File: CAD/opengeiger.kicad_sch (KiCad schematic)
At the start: 59 parts, among them J1 Conn_01x02, J10 Conn_01x04, J2 Conn_01x02, J3 Conn_01x06, J4 Conn_01x02, J5 Conn_01x04, J6 Conn_01x04, J7 Conn_01x02, J8 USB_C_Receptacle_USB2.0, J9 Conn_01x04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

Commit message: Feat:Added schematics, and updated readme
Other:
- company: (none) -> EIK IDEVERKSTED OPENGEIGER
- title: (none) -> Main Schematic
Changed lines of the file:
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@@
 (kicad_sch (version 20211123) (generator eeschema)
   (paper "A4")
+  (title_block
+    (title "Main Schematic")
+    (date "2022-11-03")
+    (rev "V.0.1.0")
+    (company "EIK IDEVERKSTED OPENGEIGER")
+  )
   (junction (at 130.81 33.02) (diameter 0) (color 0 0 0 0)
   )

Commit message: feat: added interactive html bom
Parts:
- added R18: 10k, Resistor_SMD:R_0603_1608Metric_Pad0.98x0.95mm_HandSolder, symbol Device:R
- Q3: value PMBT2222A,215 -> SI2301; MPN PMBT2222A,215 -> SI2302CDS-T1-GE3; Supplier Part Number 1727-2956-6-ND -> SI2302CDS-T1-GE3DKR-ND
- U2: INFO MOUSER -> DIGIKEY; Supplier Part Number 621-AP7361C-33ER-13 -> 576-1274-6-ND
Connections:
- net CLICKER: now also R18.2
- net GNDREF: now also R18.1
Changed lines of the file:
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@@
   (junction (at 41.91 104.14) (diameter 0) (color 0 0 0 0)
   )
+  (junction (at 198.12 62.23) (diameter 0) (color 0 0 0 0)
+  )
   (junction (at 158.75 165.1) (diameter 0) (color 0 0 0 0)
   )
@@
     (stroke (width 0) (type default) (color 0 0 0 0))
   )
+  (wire (pts (xy 198.12 62.23) (xy 200.66 62.23))
+    (stroke (width 0) (type default) (color 0 0 0 0))
+  )
   (wire (pts (xy 83.82 153.67) (xy 101.6 153.67))
     (stroke (width 0) (type default) (color 0 0 0 0))
@@
     (stroke (width 0) (type default) (color 0 0 0 0))
   )
+  (wire (pts (xy 198.12 63.5) (xy 198.12 62.23))
+    (stroke (width 0) (type default) (color 0 0 0 0))
+  )
   (wire (pts (xy 152.4 41.91) (xy 154.94 41.91))
     (stroke (width 0) (type default) (color 0 0 0 0))
@@
     (stroke (width 0) (type default) (color 0 0 0 0))
   )
+  (wire (pts (xy 195.58 62.23) (xy 198.12 62.23))
+    (stroke (width 0) (type default) (color 0 0 0 0))
+  )
   (wire (pts (xy 167.64 30.48) (xy 180.34 30.48))
     (stroke (width 0) (type default) (color 0 0 0 0))
@@
     )
   )
-  (global_label "CLICKER" (shape input) (at 200.66 62.23 180) (fields_autoplaced)
+  (global_label "CLICKER" (shape input) (at 195.58 62.23 180) (fields_autoplaced)
     (effects (font (size 1.27 1.27)) (justify right))
-    (property "Intersheet References" "${INTERSHEET_REFS}" (id 0) (at 190.385 62.1506 0)
+    (property "Intersheet References" "${INTERSHEET_REFS}" (id 0) (at 185.305 62.1506 0)
       (effects (font (size 1.27 1.27)) (justify right) hide)
     )
@@
       (effects (font (size 1.27 1.27) italic) hide)
     )
-    (property "Datasheet" "https://www.diodes.com/assets/Datasheets/AP7361C.pdf" (id 3) (at 59.69 105.41 0)
+    (property "Datasheet" "https://ww1.microchip.com/downloads/en/DeviceDoc/20005720A.pdf" (id 3) (at 59.69 105.41 0)
       (effects (font (size 1.27 1.27)) hide)
     )
@@
       (effects (font (size 1.27 1.27)) hide)
     )
-    (property "INFO" "MOUSER" (id 5) (at 59.69 104.14 0)
+    (property "INFO" "DIGIKEY" (id 5) (at 59.69 104.14 0)
       (effects (font (size 1.27 1.27)) hide)
     )
-    (property "Supplier Part Number" "621-AP7361C-33ER-13 " (id 6) (at 59.69 104.14 0)
+    (property "Supplier Part Number" "576-1274-6-ND" (id 6) (at 59.69 104.14 0)
       (effects (font (size 1.27 1.27)) hide)
     )
@@
     (pin "2")
   )
+  (symbol (lib_id "power:GNDREF") (at 198.12 71.12 0) (unit 1)
+    (in_bom yes) (on_board yes) (fields_autoplaced)
+    (property "Reference" "#PWR0112" (id 0) (at 198.12 77.47 0)
+      (effects (font (size 1.27 1.27)) hide)
+    )
+    (property "Value" "GNDREF" (id 1) (at 198.12 76.2 0))
+    (property "Footprint" "" (id 2) (at 198.12 71.12 0)
+      (effects (font (size 1.27 1.27)) hide)
+    )
+    (property "Datasheet" "" (id 3) (at 198.12 71.12 0)
+      (effects (font (size 1.27 1.27)) hide)
+    )
+    (pin "1")
+  )
   (symbol (lib_id "power:+3.3V") (at 87.63 21.59 0) (unit 1)
     (in_bom yes) (on_board yes) (fields_autoplaced)
@@
       (effects (font (size 1.27 1.27)) (justify left))
     )
-    (property "Value" "PMBT2222A,215" (id 1) (at 209.55 63.4999 0)
+    (property "Value" "SI2301" (id 1) (at 209.55 63.4999 0)
       (effects (font (size 1.27 1.27)) (justify left))
     )
@@
       (effects (font (size 1.27 1.27) italic) (justify left) hide)
     )
-    (property "Datasheet" "https://no.mouser.com/datasheet/2/916/PMBT2222A-2885992.pdf" (id 3) (at 205.74 62.23 0)
+    (property "Datasheet" "https://www.vishay.com/docs/68645/si2302cds.pdf" (id 3) (at 205.74 62.23 0)
       (effects (font (size 1.27 1.27)) (justify left) hide)
     )
-    (property "MPN" "PMBT2222A,215" (id 4) (at 205.74 62.23 0)
+    (property "MPN" "SI2302CDS-T1-GE3" (id 4) (at 205.74 62.23 0)
       (effects (font (size 1.27 1.27)) hide)
     )
@@
       (effects (font (size 1.27 1.27)) hide)
     )
-    (property "Supplier Part Number" "1727-2956-6-ND" (id 6) (at 205.74 62.23 0)
+    (property "Supplier Part Number" "SI2302CDS-T1-GE3DKR-ND" (id 6) (at 205.74 62.23 0)
       (effects (font (size 1.27 1.27)) hide)
     )
@@
     (pin "2")
   )
+  (symbol (lib_id "Device:R") (at 198.12 67.31 180) (unit 1)
+    (in_bom yes) (on_board yes) (fields_autoplaced)
+    (property "Reference" "R18" (id 0) (at 200.66 66.0399 0)
+      (effects (font (size 1.27 1.27)) (justify right))
+    )
+    (property "Value" "10k" (id 1) (at 200.66 68.5799 0)
+      (effects (font (size 1.27 1.27)) (justify right))
+    )
+    (property "Footprint" "Resistor_SMD:R_0603_1608Metric_Pad0.98x0.95mm_HandSolder" (id 2) (at 199.898 67.31 90)
+      (effects (font (size 1.27 1.27)) hide)
+    )
+    (property "Datasheet" "~" (id 3) (at 198.12 67.31 0)
+      (effects (font (size 1.27 1.27)) hide)
+    )
+    (property "MPN" "RMCF0603JT10K0" (id 4) (at 198.12 67.31 0)
+      (effects (font (size 1.27 1.27)) hide)
+    )
+    (property "INFO" "DIGIKEY" (id 5) (at 198.12 67.31 0)
+      (effects (font (size 1.27 1.27)) hide)
+    )
+    (property "Supplier Part Number" "RMCF0603JT10K0DKR-ND" (id 6) (at 198.12 67.31 0)
+      (effects (font (size 1.27 1.27)) hide)
+    )
+    (pin "1")
+    (pin "2")
+  )
   (symbol (lib_id "Device:R") (at 129.54 102.87 270) (unit 1)
     (in_bom yes) (on_board yes)
@@
       (reference "#PWR0111") (unit 1) (value "GNDREF") (footprint "")
     )
+    (path "/0aad97fa-fa3c-433f-9bf3-ad0d6000bcf6"
+      (reference "#PWR0112") (unit 1) (value "GNDREF") (footprint "")
+    )
     (path "/6395fbf7-d034-42a1-9709-4efcaf067d3b"
       (reference "#PWR0113") (unit 1) (value "GNDREF") (footprint "")
@@
     )
     (path "/6224b1eb-62ed-4248-bf78-c15c4cab3fb2"
-      (reference "Q3") (unit 1) (value "PMBT2222A,215") (footprint "Package_TO_SOT_SMD:SOT-23_Handsoldering")
+      (reference "Q3") (unit 1) (value "SI2301") (footprint "Package_TO_SOT_SMD:SOT-23_Handsoldering")
     )
     (path "/3a1001fc-93db-43cb-837e-968b85fcfe7d"
@@
       (reference "R17") (unit 1) (value "10k") (footprint "Resistor_SMD:R_0603_1608Metric_Pad0.98x0.95mm_HandSolder")
     )
+    (path "/d81c9041-9470-47cf-8392-4c5badd02a4d"
+      (reference "R18") (unit 1) (value "10k") (footprint "Resistor_SMD:R_0603_1608Metric_Pad0.98x0.95mm_HandSolder")
+    )
     (path "/2416c6cc-4624-42db-8d35-6a5410094dfa"

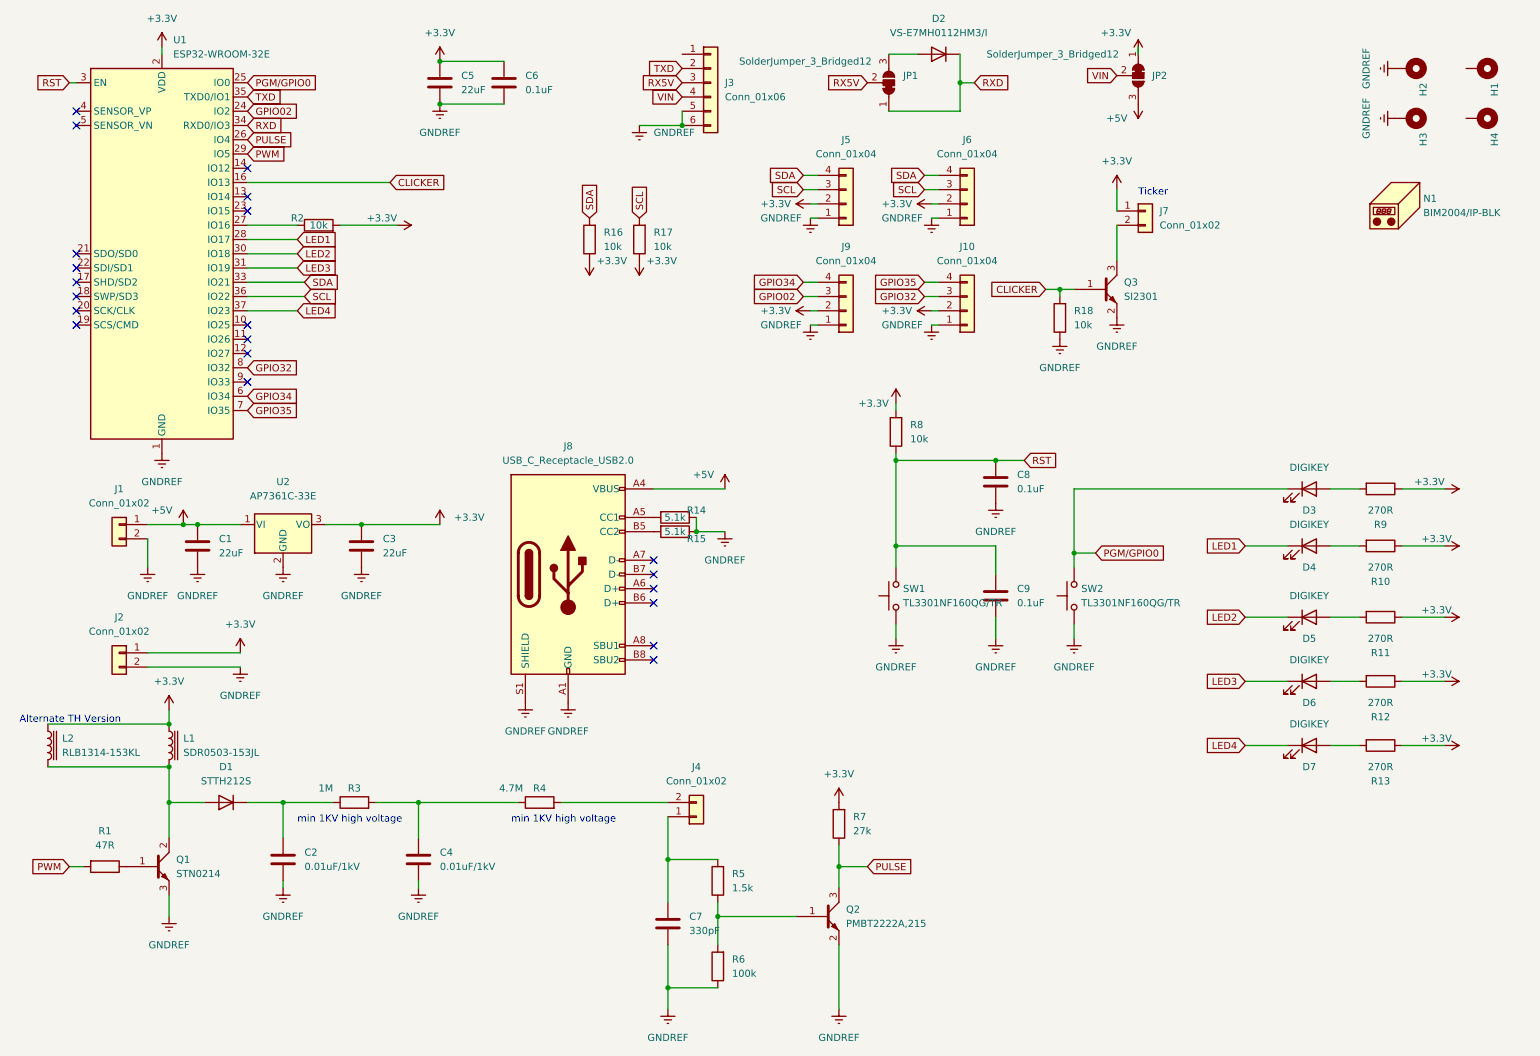
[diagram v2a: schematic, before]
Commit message: feat: 1206 version
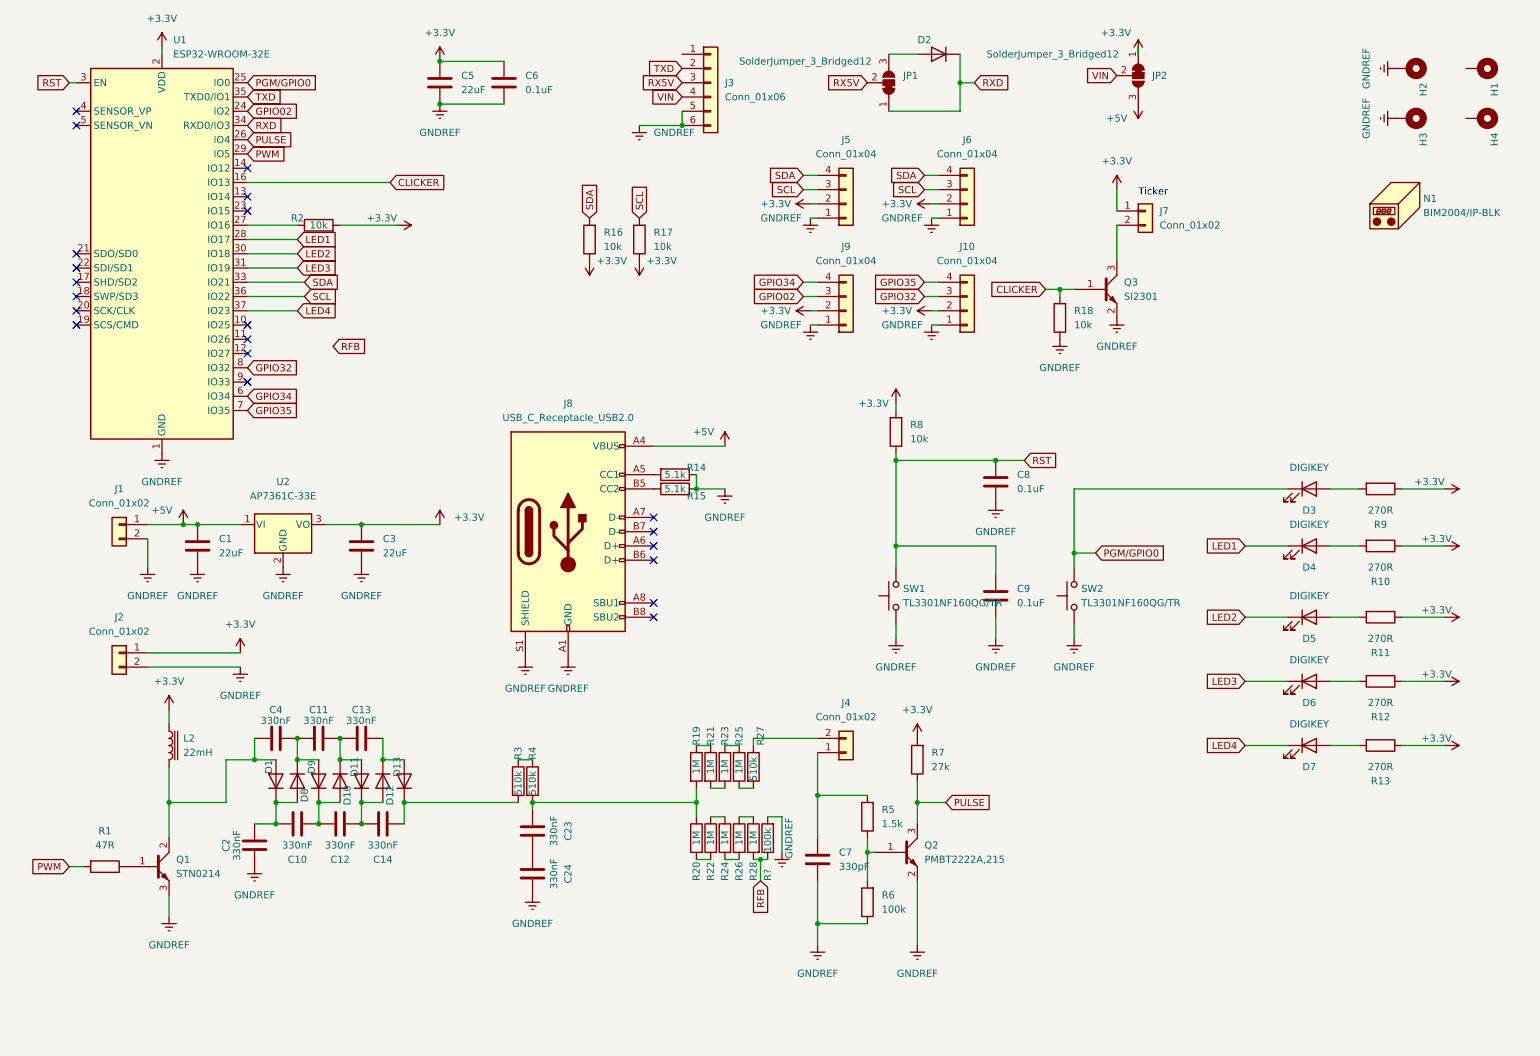
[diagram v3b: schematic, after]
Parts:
- removed L1: SDR0503-153JL, Inductor_SMD:L_TracoPower_TCK-047_5.2x5.8mm, symbol Transistors_fredrik:RLB1314-153KL
- added C10, C11, C12, C13, C14, C23, C24: 330nF, Capacitor_SMD:C_1206_3216Metric_Pad1.33x1.80mm_HandSolder, symbol Device:C
- added D10, D11, D12, D13, D8, D9: RS1J, Diode_SMD:D_SMA_Handsoldering, symbol Transistors_fredrik:SF-1200-TAP
- added R19, R20, R21, R22, R23, R24, R25, R26, R28: 1M, Resistor_SMD:R_1206_3216Metric_Pad1.30x1.75mm_HandSolder, symbol Device:R
- added R27: 510k, Resistor_SMD:R_1206_3216Metric_Pad1.30x1.75mm_HandSolder, symbol Device:R
- added R?: 100k, Resistor_SMD:R_0603_1608Metric_Pad0.98x0.95mm_HandSolder, symbol Device:R
- C2, C4: value 0.01uF/1kV -> 330nF; footprint Capacitor_SMD:C_1812_4532Metric -> Capacitor_SMD:C_1206_3216Metric_Pad1.33x1.80mm_HandSolder; MPN 1812J2K00103KXT -> CL31B333KHHSFNE; Supplier Part Number 1608-1124-1-ND -> 1276-3159-6-ND
- D1: value STTH212S -> RS1J; footprint Diode_SMD:D_SMC -> Diode_SMD:D_SMA_Handsoldering; MPN STTH212S -> RS1J; Supplier Part Number 497-4754-6-ND -> 1655-RS1JDKR-ND
- D2: value VS-E7MH0112HM3/I -> RS1J; footprint Diode_SMD:D_SMA -> Diode_SMD:D_SMA_Handsoldering; MPN VS-E7MH0112HM3/I -> RS1J; Supplier Part Number 112-VS-E7MH0112HM3/IDKR-ND -> 1655-RS1JDKR-ND
- L2: value RLB1314-153KL -> 22mH; MPN SDR0503-153JL -> RLB1014-223KL; Supplier Part Number RLB1314-153KL-ND -> RLB1014-223KL-ND
- R3: value 1M -> 510k; footprint Resistor_SMD:R_2512_6332Metric -> Resistor_SMD:R_1206_3216Metric_Pad1.30x1.75mm_HandSolder; MPN CHV2512-FX-1004ELF -> KTR18EZPJ514; Supplier Part Number CHV2512-FX-1004ELFDKR-ND -> RHM510KPDKR-ND
- R4: value 4.7M -> 510k; footprint Resistor_SMD:R_2512_6332Metric -> Resistor_SMD:R_1206_3216Metric_Pad1.30x1.75mm_HandSolder; MPN HV733ATTE475J -> KTR18EZPJ514; Supplier Part Number 2019-HV733ATTE475JDKR-ND -> RHM510KPDKR-ND
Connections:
- net GNDREF: now also C2.1, C24.1, R?.2; no longer C2.2, C4.2
- net at R4.2: now also C23.2, R19.2, R20.1; no longer J4.2 (Pin_2)
- net at D1.2 (A), L2.2, Q1.2 (C)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: now also C4.1
- new net: C12.2, C14.1, D11.1 (K), D12.2 (A)
- new net: C14.2, D13.1 (K), R3.2
- new net: R20.2, R22.2
- new net: R22.1, R24.1
- new net: R26.1, R28.1
- new net: R24.2, R26.2
- new net: C10.1, C2.2, D1.1 (K), D8.2 (A)
- new net: C10.2, C12.1, D10.2 (A), D9.1 (K)
- new net: C13.2, D12.1 (K), D13.2 (A)
- new net: C11.1, C4.2, D8.1 (K), D9.2 (A)
- new net: C11.2, C13.1, D10.1 (K), D11.2 (A)
- new net: R19.1, R21.1
- new net: R21.2, R23.2
- new net: R23.1, R25.1
- new net: J4.2 (Pin_2), R27.1
- new net: R25.2, R27.2
- new net: R3.1, R4.1
- new net: C23.1, C24.2
- new net RFB: R28.2, R?.1
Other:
- note removed: "Alternate TH Version"
- note removed: "min 1KV high voltage"
- moved on the sheet: C7, J4, J8, L2, Q2, R14, R15, R5, R6, R7

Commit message: Feat: Slimmify board
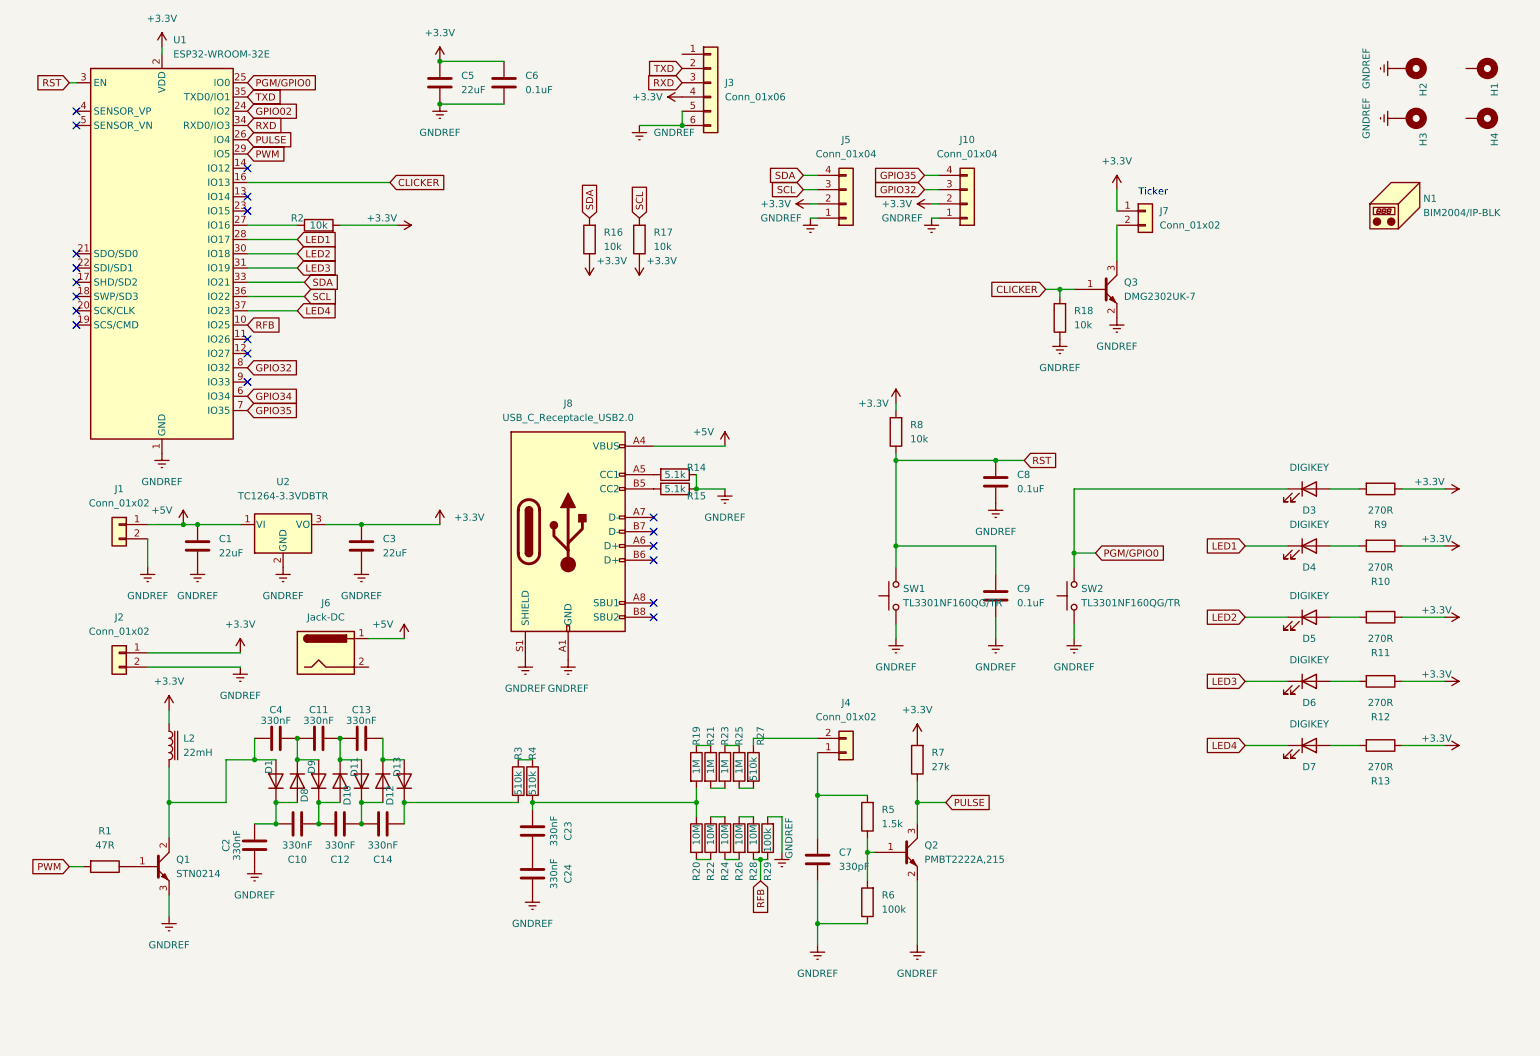
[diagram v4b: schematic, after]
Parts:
- removed D2: RS1J, Diode_SMD:D_SMA_Handsoldering, symbol Transistors_fredrik:SF-1200-TAP
- removed J6, J9: Conn_01x04, Connector_PinHeader_2.54mm:PinHeader_1x04_P2.54mm_Vertical, symbol Connector_Generic:Conn_01x04
- removed JP1, JP2: SolderJumper_3_Bridged12, Jumper:SolderJumper-3_P1.3mm_Bridged12_RoundedPad1.0x1.5mm_NumberLabels, symbol Jumper:SolderJumper_3_Bridged12
- added J6: Jack-DC, symbol Connector:Jack-DC
- Q3: value SI2301 -> DMG2302UK-7; MPN SI2302CDS-T1-GE3 -> DMG2302UK-7; Supplier Part Number SI2302CDS-T1-GE3DKR-ND -> DMG2302UK-7DIDKR-ND
- R19, R21, R23, R25: MPN KTR03EZPJ105 -> KTR18EZPF1004; Supplier Part Number RHM1.0MAZDKR-ND -> RHM1MAIDKR-ND
- R20, R22, R24, R26, R28: value 1M -> 10M; MPN KTR03EZPJ105 -> KTR18EZPF1005; Supplier Part Number RHM1.0MAZDKR-ND -> RHM10.0MAIDKR-ND
- U2: value AP7361C-33E -> TC1264-3.3VDBTR; MPN AP7361C-33E -> TC1264-3.3VDBTR; Supplier Part Number 576-1274-6-ND -> TC1264-3.3VDBDKR-ND
- gave numbers to parts that had none: 1
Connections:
- net RX5V is gone; now on net RXD: J3.3 (Pin_3)
- net VIN is gone; now on net +3.3V: J3.4 (Pin_4)
- net +5V: now also J6.1
- net RFB: now also U1.10 (IO25)
- no-connect marks 21 -> 20
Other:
- moved on the sheet: J10
